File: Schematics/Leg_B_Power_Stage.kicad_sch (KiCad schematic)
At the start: 38 parts, among them Q4 C3M0025065K, Q5 C3M0025065K, U3 UCC21710QDWRQ1, U4 UCC21710QDWRQ1

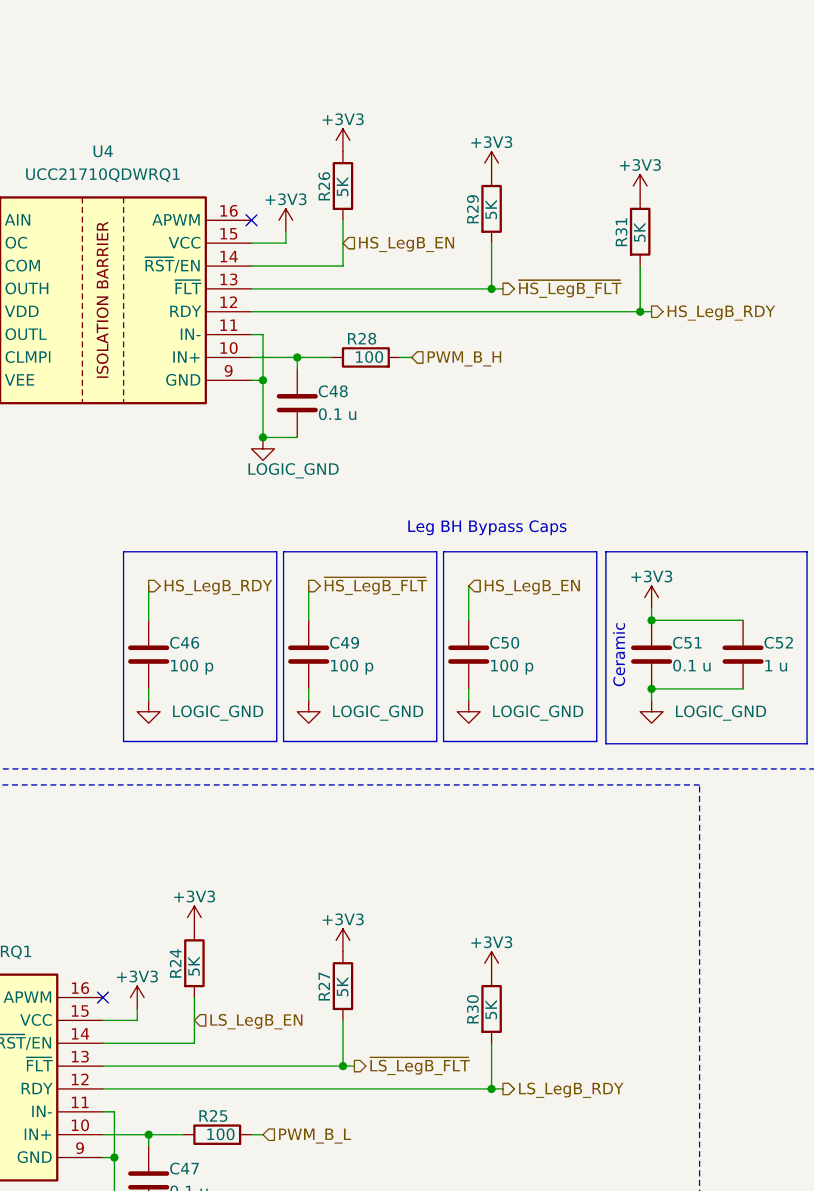
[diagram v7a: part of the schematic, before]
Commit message: WIP: Work on Controller layout, and fixed some sheet text and positions
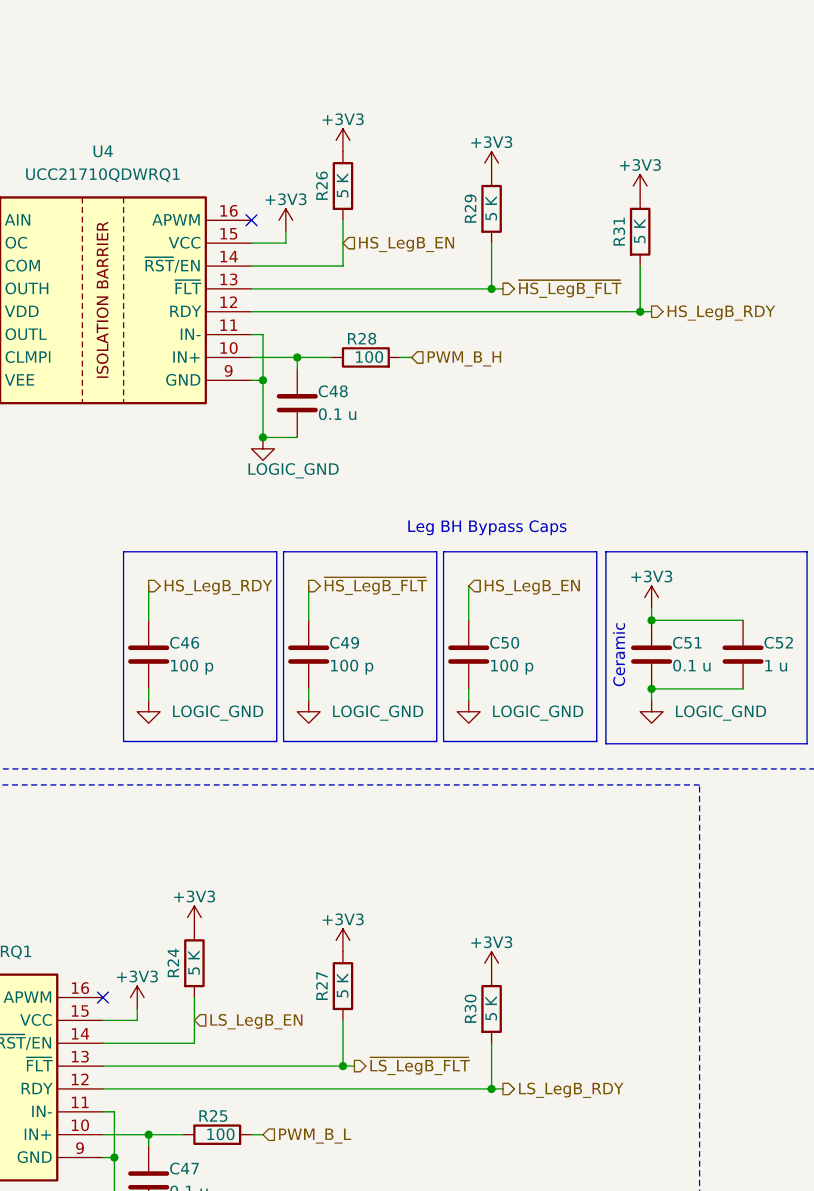
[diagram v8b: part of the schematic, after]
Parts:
- R24, R26, R27, R29, R30, R31: value 5K -> 5 K; symbol Device:R -> SiC_Inverter:RT1206BRD075KL
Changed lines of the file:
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@@
 	)
 	(symbol
-		(lib_id "Device:R")
+		(lib_id "SiC_Inverter:RT1206BRD075KL")
 		(at 207.01 133.35 0)
 		(unit 1)
@@
 		(dnp no)
 		(property "Reference" "R30"
-			(at 204.978 135.128 90)
+			(at 204.724 133.35 90)
 			(effects
 				(font
 					(size 1.27 1.27)
 				)
-				(justify left)
 			)
 		)
-		(property "Value" "5K"
-			(at 207.01 134.62 90)
+		(property "Value" "5 K"
+			(at 207.01 133.35 90)
 			(effects
 				(font
 					(size 1.27 1.27)
 				)
-				(justify left)
 			)
 		)
 		(property "Footprint" "Resistor_SMD:R_1206_3216Metric_Pad1.30x1.75mm_HandSolder"
-			(at 205.232 133.35 90)
+			(at 219.964 144.78 0)
 			(effects
 				(font
@@
 			)
 		)
-		(property "Datasheet" "~"
-			(at 207.01 133.35 0)
+		(property "Datasheet" "https://www.mouser.com/datasheet/3/508/1/PYu-RT_1-to-0.01_RoHS_L_15.pdf"
+			(at 229.362 147.066 0)
 			(effects
 				(font
@@
 			)
 		)
-		(property "Description" "Resistor"
-			(at 207.01 133.35 0)
+		(property "Description" "Thin Film Resistors - SMD 1/4W 5K ohm .1% 25ppm"
+			(at 215.646 149.352 0)
 			(effects
 				(font
@@
 	)
 	(symbol
-		(lib_id "Device:R")
+		(lib_id "SiC_Inverter:RT1206BRD075KL")
 		(at 223.52 46.99 0)
 		(unit 1)
@@
 		(dnp no)
 		(property "Reference" "R31"
-			(at 221.488 48.768 90)
+			(at 221.234 46.99 90)
 			(effects
 				(font
 					(size 1.27 1.27)
 				)
-				(justify left)
 			)
 		)
-		(property "Value" "5K"
-			(at 223.52 48.26 90)
+		(property "Value" "5 K"
+			(at 223.52 46.99 90)
 			(effects
 				(font
 					(size 1.27 1.27)
 				)
-				(justify left)
 			)
 		)
 		(property "Footprint" "Resistor_SMD:R_1206_3216Metric_Pad1.30x1.75mm_HandSolder"
-			(at 221.742 46.99 90)
+			(at 236.474 58.42 0)
 			(effects
 				(font
@@
 			)
 		)
-		(property "Datasheet" "~"
-			(at 223.52 46.99 0)
+		(property "Datasheet" "https://www.mouser.com/datasheet/3/508/1/PYu-RT_1-to-0.01_RoHS_L_15.pdf"
+			(at 245.872 60.706 0)
 			(effects
 				(font
@@
 			)
 		)
-		(property "Description" "Resistor"
-			(at 223.52 46.99 0)
+		(property "Description" "Thin Film Resistors - SMD 1/4W 5K ohm .1% 25ppm"
+			(at 232.156 62.992 0)
 			(effects
 				(font
@@
 	)
 	(symbol
-		(lib_id "Device:R")
+		(lib_id "SiC_Inverter:RT1206BRD075KL")
 		(at 207.01 44.45 0)
 		(unit 1)
@@
 		(dnp no)
 		(property "Reference" "R29"
-			(at 204.978 46.228 90)
+			(at 204.724 44.45 90)
 			(effects
 				(font
 					(size 1.27 1.27)
 				)
-				(justify left)
 			)
 		)
-		(property "Value" "5K"
-			(at 207.01 45.72 90)
+		(property "Value" "5 K"
+			(at 207.01 44.45 90)
 			(effects
 				(font
 					(size 1.27 1.27)
 				)
-				(justify left)
 			)
 		)
 		(property "Footprint" "Resistor_SMD:R_1206_3216Metric_Pad1.30x1.75mm_HandSolder"
-			(at 205.232 44.45 90)
+			(at 219.964 55.88 0)
 			(effects
 				(font
@@
 			)
 		)
-		(property "Datasheet" "~"
-			(at 207.01 44.45 0)
+		(property "Datasheet" "https://www.mouser.com/datasheet/3/508/1/PYu-RT_1-to-0.01_RoHS_L_15.pdf"
+			(at 229.362 58.166 0)
 			(effects
 				(font
@@
 			)
 		)
-		(property "Description" "Resistor"
-			(at 207.01 44.45 0)
+		(property "Description" "Thin Film Resistors - SMD 1/4W 5K ohm .1% 25ppm"
+			(at 215.646 60.452 0)
 			(effects
 				(font
@@
 	)
 	(symbol
-		(lib_id "Device:R")
+		(lib_id "SiC_Inverter:RT1206BRD075KL")
 		(at 173.99 128.27 0)
 		(unit 1)
@@
 		(dnp no)
 		(property "Reference" "R24"
-			(at 171.958 130.048 90)
+			(at 171.704 128.27 90)
 			(effects
 				(font
 					(size 1.27 1.27)
 				)
-				(justify left)
 			)
 		)
-		(property "Value" "5K"
-			(at 173.99 129.794 90)
+		(property "Value" "5 K"
+			(at 173.99 128.27 90)
 			(effects
 				(font
 					(size 1.27 1.27)
 				)
-				(justify left)
 			)
 		)
 		(property "Footprint" "Resistor_SMD:R_1206_3216Metric_Pad1.30x1.75mm_HandSolder"
-			(at 172.212 128.27 90)
+			(at 186.944 139.7 0)
 			(effects
 				(font
@@
 			)
 		)
-		(property "Datasheet" "~"
-			(at 173.99 128.27 0)
+		(property "Datasheet" "https://www.mouser.com/datasheet/3/508/1/PYu-RT_1-to-0.01_RoHS_L_15.pdf"
+			(at 196.342 141.986 0)
 			(effects
 				(font
@@
 			)
 		)
-		(property "Description" "Resistor"
-			(at 173.99 128.27 0)
+		(property "Description" "Thin Film Resistors - SMD 1/4W 5K ohm .1% 25ppm"
+			(at 182.626 144.272 0)
 			(effects
 				(font
@@
 	)
 	(symbol
-		(lib_id "Device:R")
+		(lib_id "SiC_Inverter:RT1206BRD075KL")
 		(at 190.5 41.91 0)
 		(unit 1)
@@
 		(dnp no)
 		(property "Reference" "R26"
-			(at 188.468 43.688 90)
+			(at 188.214 41.91 90)
 			(effects
 				(font
 					(size 1.27 1.27)
 				)
-				(justify left)
 			)
 		)
-		(property "Value" "5K"
-			(at 190.5 43.18 90)
+		(property "Value" "5 K"
+			(at 190.5 41.91 90)
 			(effects
 				(font
 					(size 1.27 1.27)
 				)
-				(justify left)
 			)
 		)
 		(property "Footprint" "Resistor_SMD:R_1206_3216Metric_Pad1.30x1.75mm_HandSolder"
-			(at 188.722 41.91 90)
+			(at 203.454 53.34 0)
 			(effects
 				(font
@@
 			)
 		)
-		(property "Datasheet" "~"
-			(at 190.5 41.91 0)
+		(property "Datasheet" "https://www.mouser.com/datasheet/3/508/1/PYu-RT_1-to-0.01_RoHS_L_15.pdf"
+			(at 212.852 55.626 0)
 			(effects
 				(font
@@
 			)
 		)
-		(property "Description" "Resistor"
-			(at 190.5 41.91 0)
+		(property "Description" "Thin Film Resistors - SMD 1/4W 5K ohm .1% 25ppm"
+			(at 199.136 57.912 0)
 			(effects
 				(font
@@
 	)
 	(symbol
-		(lib_id "Device:R")
+		(lib_id "SiC_Inverter:RT1206BRD075KL")
 		(at 190.5 130.81 0)
 		(unit 1)
@@
 		(dnp no)
 		(property "Reference" "R27"
-			(at 188.468 132.588 90)
+			(at 188.214 130.81 90)
 			(effects
 				(font
 					(size 1.27 1.27)
 				)
-				(justify left)
 			)
 		)
-		(property "Value" "5K"
-			(at 190.5 132.08 90)
+		(property "Value" "5 K"
+			(at 190.5 130.81 90)
 			(effects
 				(font
 					(size 1.27 1.27)
 				)
-				(justify left)
 			)
 		)
 		(property "Footprint" "Resistor_SMD:R_1206_3216Metric_Pad1.30x1.75mm_HandSolder"
-			(at 188.722 130.81 90)
+			(at 203.454 142.24 0)
 			(effects
 				(font
@@
 			)
 		)
-		(property "Datasheet" "~"
-			(at 190.5 130.81 0)
+		(property "Datasheet" "https://www.mouser.com/datasheet/3/508/1/PYu-RT_1-to-0.01_RoHS_L_15.pdf"
+			(at 212.852 144.526 0)
 			(effects
 				(font
@@
 			)
 		)
-		(property "Description" "Resistor"
-			(at 190.5 130.81 0)
+		(property "Description" "Thin Film Resistors - SMD 1/4W 5K ohm .1% 25ppm"
+			(at 199.136 146.812 0)
 			(effects
 				(font
